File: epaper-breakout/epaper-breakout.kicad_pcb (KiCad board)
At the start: 2 copper layers, 81.3 x 69.8 mm, 63 parts, among them J1 XF2M-3315-1A, J2 C10418, J3 Conn_01x10, Q1 IRLML6402, U1 LT1086-3.3, U2 LT1945, U3 L7915, U4 L7815, U5 ESP32-WROOM-32, U6 CH330N, U7 LM358

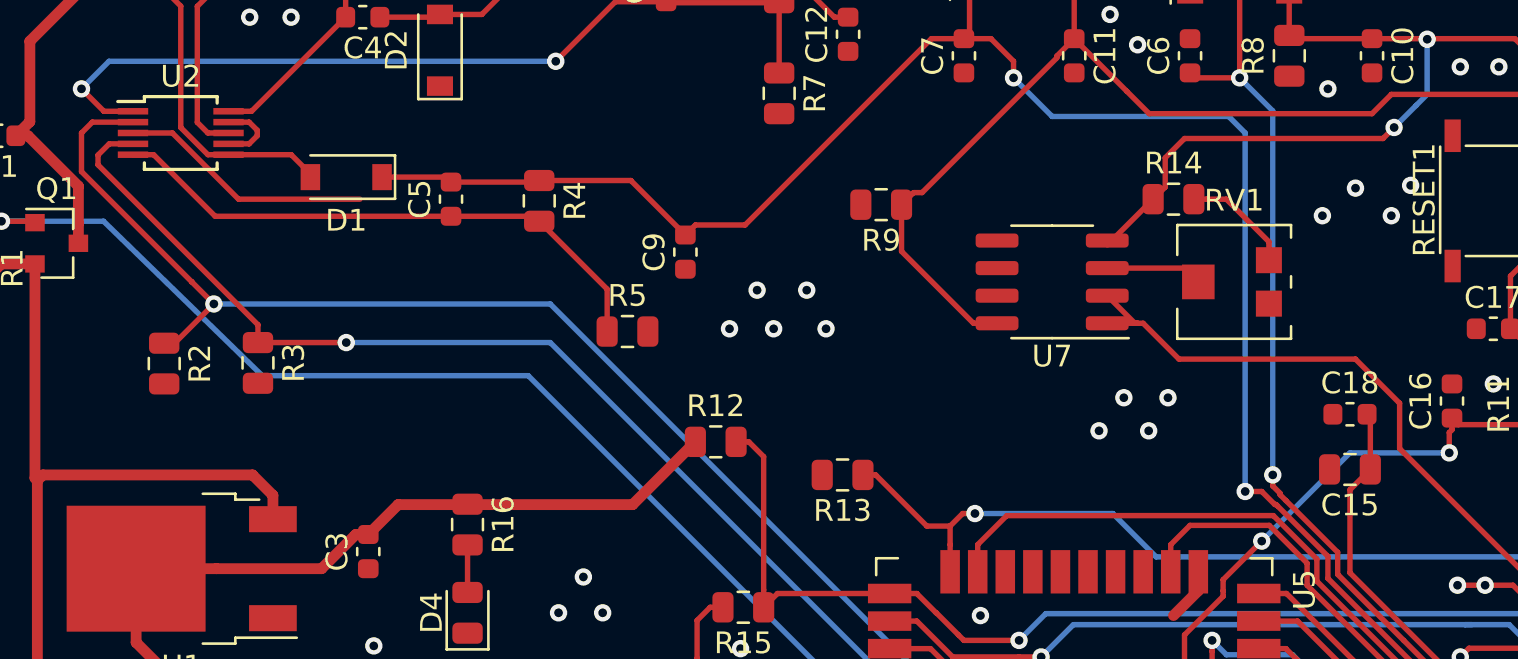
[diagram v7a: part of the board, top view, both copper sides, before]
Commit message: fix weird fill near u2
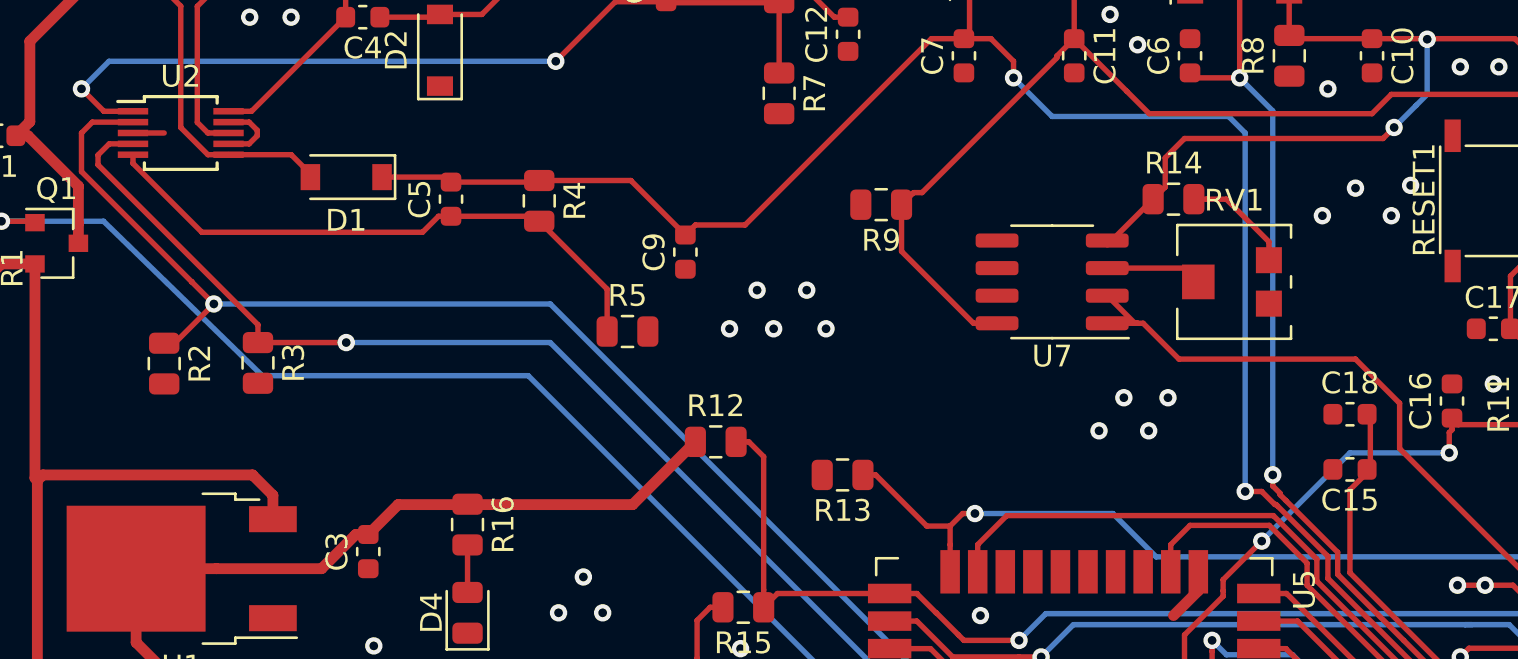
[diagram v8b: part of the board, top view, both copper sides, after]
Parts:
- C15: value 100uF -> 10uF; footprint Capacitor_SMD:C_0805_2012Metric -> Capacitor_SMD:C_0603_1608Metric
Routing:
- net GND: track 45.7 -> 35.4 mm
- net Net-(C5-Pad1): track 26.4 -> 27.2 mm
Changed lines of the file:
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@@
   )
   (setup
-    (last_trace_width 0.5)
+    (last_trace_width 0.25)
     (user_trace_width 0.5)
     (trace_clearance 0.2)
@@
     (add_net "Net-(U6-Pad4)")
   )
+  (module Capacitor_SMD:C_0603_1608Metric (layer F.Cu)
+    (at 117.348 -94.234 180)
+    (descr "Capacitor SMD 0603 (1608 Metric), square (rectangular) end terminal, IPC_7351 nominal, (Body size source: http://www.tortai-tech.com/upload/download/2011102023233369053.pdf), generated with kicad-footprint-generator")
+    (tags capacitor)
+    (attr smd)
+    (fp_text reference C15 (at 0 -1.43) (layer F.SilkS)
+      (effects (font (size 1 1) (thickness 0.15)))
+    )
+    (fp_text value 10uF (at 0 1.43) (layer F.Fab)
+      (effects (font (size 1 1) (thickness 0.15)))
+    )
+    (fp_text user %R (at 0 0) (layer F.Fab)
+      (effects (font (size 0.4 0.4) (thickness 0.06)))
+    )
+    (fp_line (start 1.48 0.73) (end -1.48 0.73) (layer F.CrtYd) (width 0.05))
+    (fp_line (start 1.48 -0.73) (end 1.48 0.73) (layer F.CrtYd) (width 0.05))
+    (fp_line (start -1.48 -0.73) (end 1.48 -0.73) (layer F.CrtYd) (width 0.05))
+    (fp_line (start -1.48 0.73) (end -1.48 -0.73) (layer F.CrtYd) (width 0.05))
+    (fp_line (start -0.162779 0.51) (end 0.162779 0.51) (layer F.SilkS) (width 0.12))
+    (fp_line (start -0.162779 -0.51) (end 0.162779 -0.51) (layer F.SilkS) (width 0.12))
+    (fp_line (start 0.8 0.4) (end -0.8 0.4) (layer F.Fab) (width 0.1))
+    (fp_line (start 0.8 -0.4) (end 0.8 0.4) (layer F.Fab) (width 0.1))
+    (fp_line (start -0.8 -0.4) (end 0.8 -0.4) (layer F.Fab) (width 0.1))
+    (fp_line (start -0.8 0.4) (end -0.8 -0.4) (layer F.Fab) (width 0.1))
+    (pad 2 smd roundrect (at 0.7875 0 180) (size 0.875 0.95) (layers F.Cu F.Paste F.Mask) (roundrect_rratio 0.25)
+      (net 1 GND))
+    (pad 1 smd roundrect (at -0.7875 0 180) (size 0.875 0.95) (layers F.Cu F.Paste F.Mask) (roundrect_rratio 0.25)
+      (net 4 /+3.3V))
+    (model ${KISYS3DMOD}/Capacitor_SMD.3dshapes/C_0603_1608Metric.wrl
+      (at (xyz 0 0 0))
+      (scale (xyz 1 1 1))
+      (rotate (xyz 0 0 0))
+    )
+  )
   (module MountingHole:MountingHole_2.2mm_M2 (layer F.Cu)
     (at 55 -120)
@@
     )
   )
-  (module Capacitor_SMD:C_0805_2012Metric (layer F.Cu)
-    (at 117.348 -94.234 180)
-    (descr "Capacitor SMD 0805 (2012 Metric), square (rectangular) end terminal, IPC_7351 nominal, (Body size source: https://docs.google.com/spreadsheets/d/1BsfQQcO9C6DZCsRaXUlFlo91Tg2WpOkGARC1WS5S8t0/edit?usp=sharing), generated with kicad-footprint-generator")
-    (tags capacitor)
-    (attr smd)
-    (fp_text reference C15 (at 0 -1.65) (layer F.SilkS)
-      (effects (font (size 1 1) (thickness 0.15)))
-    )
-    (fp_text value 100uF (at 0 1.65) (layer F.Fab)
-      (effects (font (size 1 1) (thickness 0.15)))
-    )
-    (fp_text user %R (at 0 0) (layer F.Fab)
-      (effects (font (size 0.5 0.5) (thickness 0.08)))
-    )
-    (fp_line (start 1.68 0.95) (end -1.68 0.95) (layer F.CrtYd) (width 0.05))
-    (fp_line (start 1.68 -0.95) (end 1.68 0.95) (layer F.CrtYd) (width 0.05))
-    (fp_line (start -1.68 -0.95) (end 1.68 -0.95) (layer F.CrtYd) (width 0.05))
-    (fp_line (start -1.68 0.95) (end -1.68 -0.95) (layer F.CrtYd) (width 0.05))
-    (fp_line (start -0.258578 0.71) (end 0.258578 0.71) (layer F.SilkS) (width 0.12))
-    (fp_line (start -0.258578 -0.71) (end 0.258578 -0.71) (layer F.SilkS) (width 0.12))
-    (fp_line (start 1 0.6) (end -1 0.6) (layer F.Fab) (width 0.1))
-    (fp_line (start 1 -0.6) (end 1 0.6) (layer F.Fab) (width 0.1))
-    (fp_line (start -1 -0.6) (end 1 -0.6) (layer F.Fab) (width 0.1))
-    (fp_line (start -1 0.6) (end -1 -0.6) (layer F.Fab) (width 0.1))
-    (pad 2 smd roundrect (at 0.9375 0 180) (size 0.975 1.4) (layers F.Cu F.Paste F.Mask) (roundrect_rratio 0.25)
-      (net 1 GND))
-    (pad 1 smd roundrect (at -0.9375 0 180) (size 0.975 1.4) (layers F.Cu F.Paste F.Mask) (roundrect_rratio 0.25)
-      (net 4 /+3.3V))
-    (model ${KISYS3DMOD}/Capacitor_SMD.3dshapes/C_0805_2012Metric.wrl
-      (at (xyz 0 0 0))
-      (scale (xyz 1 1 1))
-      (rotate (xyz 0 0 0))
-    )
-  )
   (module Capacitor_SMD:C_0603_1608Metric (layer F.Cu)
     (at 78.7145 -79.756)
@@
   (segment (start 67.023 -109.601) (end 67.023 -109.855) (width 0.25) (layer F.Cu) (net 1))
   (segment (start 65.7 -109.228) (end 66.65 -109.228) (width 0.25) (layer F.Cu) (net 1))
-  (segment (start 63.11359 -109.728) (end 66.16159 -106.68) (width 0.25) (layer F.Cu) (net 1))
-  (segment (start 61.3 -109.728) (end 63.11359 -109.728) (width 0.25) (layer F.Cu) (net 1))
-  (segment (start 66.16159 -106.68) (end 71.755 -106.68) (width 0.25) (layer F.Cu) (net 1))
   (segment (start 55.278 -73.884) (end 56.926 -73.884) (width 0.5) (layer F.Cu) (net 1))
   (via (at 121.793 -72.39) (size 0.8) (drill 0.4) (layers F.Cu B.Cu) (net 1))
   (via (at 122.682 -71.12) (size 0.8) (drill 0.4) (layers F.Cu B.Cu) (net 1))
   (via (at 123.317 -72.39) (size 0.8) (drill 0.4) (layers F.Cu B.Cu) (net 1))
+  (segment (start 61.3 -109.728) (end 62.738 -109.728) (width 0.25) (layer F.Cu) (net 1))
   (segment (start 64.75 -109.728) (end 65.7 -109.728) (width 0.25) (layer F.Cu) (net 2))
   (segment (start 64.262 -110.216) (end 64.75 -109.728) (width 0.25) (layer F.Cu) (net 2))
@@
   (segment (start 84.231 -107.539) (end 86.741 -105.029) (width 0.25) (layer F.Cu) (net 7))
   (segment (start 80.01 -107.539) (end 84.231 -107.539) (width 0.25) (layer F.Cu) (net 7))
-  (segment (start 65.0855 -105.8925) (end 75.946 -105.8925) (width 0.25) (layer F.Cu) (net 8))
-  (segment (start 61.3 -108.728) (end 62.25 -108.728) (width 0.25) (layer F.Cu) (net 8))
-  (segment (start 62.25 -108.728) (end 65.0855 -105.8925) (width 0.25) (layer F.Cu) (net 8))
   (segment (start 79.7815 -105.8925) (end 80.01 -105.664) (width 0.25) (layer F.Cu) (net 8))
   (segment (start 75.946 -105.8925) (end 79.7815 -105.8925) (width 0.25) (layer F.Cu) (net 8))
   (segment (start 83.1365 -102.5375) (end 83.1365 -100.584) (width 0.25) (layer F.Cu) (net 8))
   (segment (start 80.01 -105.664) (end 83.1365 -102.5375) (width 0.25) (layer F.Cu) (net 8))
+  (segment (start 64.472 -105.156) (end 61.3 -108.328) (width 0.25) (layer F.Cu) (net 8))
+  (segment (start 74.6345 -105.156) (end 64.472 -105.156) (width 0.25) (layer F.Cu) (net 8))
+  (segment (start 75.371 -105.8925) (end 74.6345 -105.156) (width 0.25) (layer F.Cu) (net 8))
+  (segment (start 61.3 -108.328) (end 61.3 -108.728) (width 0.25) (layer F.Cu) (net 8))
+  (segment (start 75.946 -105.8925) (end 75.371 -105.8925) (width 0.25) (layer F.Cu) (net 8))
   (segment (start 122.688231 -83.494001) (end 119.822232 -86.36) (width 0.25) (layer F.Cu) (net 9))
   (segment (start 127.4191 -83.494001) (end 122.688231 -83.494001) (width 0.25) (layer F.Cu) (net 9))
@@
   (segment (start 125.827 -104.601) (end 125.827 -109.601) (width 0.25) (layer F.Cu) (net 14))
   (segment (start 125.827 -103.601) (end 125.827 -104.601) (width 0.25) (layer F.Cu) (net 14))
-  (segment (start 87.279 -85.534) (end 87.279 -84.534) (width 0.25) (layer F.Cu) (net 66))
-  (segment (start 87.279 -87.28) (end 87.279 -85.534) (width 0.25) (layer F.Cu) (net 66))
-  (segment (start 87.883 -87.884) (end 87.279 -87.28) (width 0.25) (layer F.Cu) (net 66))
-  (segment (start 88.4705 -87.884) (end 87.883 -87.884) (width 0.25) (layer F.Cu) (net 66))
-  (segment (start 87.279 -84.534) (end 87.279 -78.534) (width 0.25) (layer F.Cu) (net 66))
-  (segment (start 87.279 -76.424) (end 88.519 -75.184) (width 0.25) (layer F.Cu) (net 66))
-  (segment (start 87.279 -78.534) (end 87.279 -76.424) (width 0.25) (layer F.Cu) (net 66))
   (segment (start 65.7 -108.728) (end 64.75 -108.728) (width 0.25) (layer F.Cu) (net 15))
   (segment (start 69.47 -107.846) (end 69.47 -107.696) (width 0.25) (layer F.Cu) (net 15))
@@
   (segment (start 63.5 -115.57) (end 61.512 -117.558) (width 0.25) (layer F.Cu) (net 15))
   (segment (start 76.708 -90.7565) (end 76.708 -88.5675) (width 0.25) (layer F.Cu) (net 16))
-  (segment (start 66.8815 -67.056) (end 69.469 -67.056) (width 0.25) (layer F.Cu) (net 67))
-  (segment (start 66.294 -67.056) (end 66.8815 -67.056) (width 0.25) (layer F.Cu) (net 67))
-  (segment (start 68.9115 -70.612) (end 66.294 -70.612) (width 0.25) (layer F.Cu) (net 68))
-  (segment (start 69.499 -70.612) (end 68.9115 -70.612) (width 0.25) (layer F.Cu) (net 68))
   (segment (start 96.148 -73.279) (end 107.823 -73.279) (width 0.25) (layer F.Cu) (net 20))
   (segment (start 107.823 -73.279) (end 107.823 -73.279) (width 0.25) (layer F.Cu) (net 20))
@@
   (segment (start 109.729 -103.505) (end 110.364 -102.87) (width 0.25) (layer F.Cu) (net 57))
   (segment (start 106.1695 -103.505) (end 109.729 -103.505) (width 0.25) (layer F.Cu) (net 57))
+  (segment (start 87.279 -85.534) (end 87.279 -84.534) (width 0.25) (layer F.Cu) (net 66))
+  (segment (start 87.279 -87.28) (end 87.279 -85.534) (width 0.25) (layer F.Cu) (net 66))
+  (segment (start 87.883 -87.884) (end 87.279 -87.28) (width 0.25) (layer F.Cu) (net 66))
+  (segment (start 88.4705 -87.884) (end 87.883 -87.884) (width 0.25) (layer F.Cu) (net 66))
+  (segment (start 87.279 -84.534) (end 87.279 -78.534) (width 0.25) (layer F.Cu) (net 66))
+  (segment (start 87.279 -76.424) (end 88.519 -75.184) (width 0.25) (layer F.Cu) (net 66))
+  (segment (start 87.279 -78.534) (end 87.279 -76.424) (width 0.25) (layer F.Cu) (net 66))
+  (segment (start 66.8815 -67.056) (end 69.469 -67.056) (width 0.25) (layer F.Cu) (net 67))
+  (segment (start 66.294 -67.056) (end 66.8815 -67.056) (width 0.25) (layer F.Cu) (net 67))
+  (segment (start 68.9115 -70.612) (end 66.294 -70.612) (width 0.25) (layer F.Cu) (net 68))
+  (segment (start 69.499 -70.612) (end 68.9115 -70.612) (width 0.25) (layer F.Cu) (net 68))
   (zone (net 1) (net_name GND) (layer F.Cu) (hatch edge 0.508)
     (connect_pads (clearance 0.508))
